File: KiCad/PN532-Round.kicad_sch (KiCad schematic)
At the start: 52 parts, among them J1 Bell, J2 SPOX, SW1 TAMPER, U1 PN532, U2 QR, U3 QR, Y1 27.12MHz

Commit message: Better antennna
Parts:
- removed U3: QR, RevK:QR-PN532, symbol RevK:QR
- added J2: Bell, RevK:PinHeader_1x02_P2.54mm_Vertical_SMD_Pin1Left, symbol Connector:Conn_01x02_Male
- J1: footprint RevK:PinHeader_1x02_P2.54mm_Vertical -> RevK:PinHeader_1x02_P2.54mm_Vertical_SMD_Pin1Right
- J3: renamed from J2; footprint RevK:Molex_MiniSPOX_H4V -> RevK:PinHeader_1x04_P2.54mm_Vertical_SMD_Pin1Right
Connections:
- net GND: now also J2.1 (Pin_1)
- net at R11.2, SW1.2, U1.24 (P30/UART_RX): now also J2.2 (Pin_2)
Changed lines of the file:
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@@
   (junction (at 128.27 118.11) (diameter 0) (color 0 0 0 0)
+  )
+  (junction (at 224.79 25.4) (diameter 0) (color 0 0 0 0)
   )
   (junction (at 231.14 119.38) (diameter 0) (color 0 0 0 0)
@@
     (stroke (width 0) (type default) (color 0 0 0 0))
   )
+  (wire (pts (xy 224.79 25.4) (xy 234.95 25.4))
+    (stroke (width 0) (type default) (color 0 0 0 0))
+  )
   (wire (pts (xy 170.18 74.93) (xy 170.18 80.01))
     (stroke (width 0) (type default) (color 0 0 0 0))
@@
     (stroke (width 0) (type default) (color 0 0 0 0))
   )
-  (wire (pts (xy 224.79 20.32) (xy 224.79 92.71))
-    (stroke (width 0) (type default) (color 0 0 0 0))
-  )
   (wire (pts (xy 237.49 152.4) (xy 246.38 152.4))
     (stroke (width 0) (type default) (color 0 0 0 0))
@@
     (stroke (width 0) (type default) (color 0 0 0 0))
   )
+  (wire (pts (xy 224.79 25.4) (xy 224.79 92.71))
+    (stroke (width 0) (type default) (color 0 0 0 0))
+  )
   (wire (pts (xy 138.43 115.57) (xy 133.35 115.57))
     (stroke (width 0) (type default) (color 0 0 0 0))
@@
   )
   (wire (pts (xy 133.35 115.57) (xy 133.35 127))
+    (stroke (width 0) (type default) (color 0 0 0 0))
+  )
+  (wire (pts (xy 224.79 20.32) (xy 224.79 25.4))
     (stroke (width 0) (type default) (color 0 0 0 0))
   )
@@
   (symbol (lib_id "Connector:Conn_01x04_Male") (at 247.65 78.74 0) (unit 1)
     (in_bom no) (on_board yes)
-    (property "Reference" "J2" (id 0) (at 250.3932 71.6026 0))
+    (property "Reference" "J3" (id 0) (at 250.3932 71.6026 0))
     (property "Value" "SPOX" (id 1) (at 250.3932 73.914 0))
-    (property "Footprint" "RevK:Molex_MiniSPOX_H4V" (id 2) (at 247.65 78.74 0)
+    (property "Footprint" "RevK:PinHeader_1x04_P2.54mm_Vertical_SMD_Pin1Right" (id 2) (at 247.65 78.74 0)
       (effects (font (size 1.27 1.27)) hide)
     )
@@
   (symbol (lib_id "power:GND") (at 252.73 76.2 90) (unit 1)
     (in_bom yes) (on_board yes)
-    (property "Reference" "#PWR041" (id 0) (at 259.08 76.2 0)
+    (property "Reference" "#PWR042" (id 0) (at 259.08 76.2 0)
       (effects (font (size 1.27 1.27)) hide)
     )
@@
   (symbol (lib_id "power:+5V") (at 252.73 78.74 270) (unit 1)
     (in_bom yes) (on_board yes)
-    (property "Reference" "#PWR042" (id 0) (at 248.92 78.74 0)
+    (property "Reference" "#PWR043" (id 0) (at 248.92 78.74 0)
       (effects (font (size 1.27 1.27)) hide)
     )
@@
     (property "Reference" "J1" (id 0) (at 214.8332 145.2626 0))
     (property "Value" "Bell" (id 1) (at 214.8332 147.574 0))
-    (property "Footprint" "RevK:PinHeader_1x02_P2.54mm_Vertical" (id 2) (at 212.09 149.86 0)
+    (property "Footprint" "RevK:PinHeader_1x02_P2.54mm_Vertical_SMD_Pin1Right" (id 2) (at 212.09 149.86 0)
       (effects (font (size 1.27 1.27)) hide)
     )
@@
     )
     (pin "1")
-  )
-  (symbol (lib_id "RevK:QR") (at 281.305 173.355 0) (unit 1)
-    (in_bom no) (on_board yes)
-    (property "Reference" "U3" (id 0) (at 281.305 174.625 0)
-      (effects (font (size 1.27 1.27)) hide)
-    )
-    (property "Value" "QR" (id 1) (at 281.305 174.625 0)
-      (effects (font (size 1.27 1.27)) hide)
-    )
-    (property "Footprint" "RevK:QR-PN532" (id 2) (at 281.305 173.355 0)
-      (effects (font (size 1.27 1.27)) hide)
-    )
-    (property "Datasheet" "" (id 3) (at 281.305 173.355 0)
-      (effects (font (size 1.27 1.27)) hide)
-    )
-    (property "Note" "Non part, PCB printed" (id 4) (at 281.305 173.355 0)
-      (effects (font (size 1.27 1.27)) hide)
-    )
   )
   (symbol (lib_id "Device:R") (at 250.19 152.4 270) (unit 1)
@@
   (symbol (lib_id "power:+3.3V") (at 254 152.4 270) (unit 1)
     (in_bom yes) (on_board yes)
-    (property "Reference" "#PWR043" (id 0) (at 250.19 152.4 0)
+    (property "Reference" "#PWR044" (id 0) (at 250.19 152.4 0)
       (effects (font (size 1.27 1.27)) hide)
     )
@@
   (symbol (lib_id "power:GND") (at 238.76 105.41 0) (mirror y) (unit 1)
     (in_bom yes) (on_board yes)
-    (property "Reference" "#PWR040" (id 0) (at 238.76 111.76 0)
+    (property "Reference" "#PWR041" (id 0) (at 238.76 111.76 0)
       (effects (font (size 1.27 1.27)) hide)
     )
@@
   (symbol (lib_id "power:+3.3V") (at 238.76 90.17 0) (mirror y) (unit 1)
     (in_bom yes) (on_board yes)
-    (property "Reference" "#PWR039" (id 0) (at 238.76 93.98 0)
+    (property "Reference" "#PWR040" (id 0) (at 238.76 93.98 0)
       (effects (font (size 1.27 1.27)) hide)
     )
@@
   (symbol (lib_id "power:GND") (at 234.95 127 0) (unit 1)
     (in_bom yes) (on_board yes)
-    (property "Reference" "#PWR038" (id 0) (at 234.95 133.35 0)
+    (property "Reference" "#PWR039" (id 0) (at 234.95 133.35 0)
       (effects (font (size 1.27 1.27)) hide)
     )
@@
     (pin "~")
   )
+  (symbol (lib_id "power:GND") (at 234.95 27.94 270) (unit 1)
+    (in_bom yes) (on_board yes) (fields_autoplaced)
+    (property "Reference" "#PWR038" (id 0) (at 228.6 27.94 0)
+      (effects (font (size 1.27 1.27)) hide)
+    )
+    (property "Value" "GND" (id 1) (at 231.7751 28.3738 90)
+      (effects (font (size 1.27 1.27)) (justify right))
+    )
+    (property "Footprint" "" (id 2) (at 234.95 27.94 0)
+      (effects (font (size 1.27 1.27)) hide)
+    )
+    (property "Datasheet" "" (id 3) (at 234.95 27.94 0)
+      (effects (font (size 1.27 1.27)) hide)
+    )
+    (pin "1")
+  )
   (symbol (lib_name "Cx2_1") (lib_id "RevK:Cx2") (at 64.77 107.95 0) (unit 1)
     (in_bom yes) (on_board yes)
@@
     )
     (pin "~")
+  )
+  (symbol (lib_id "Connector:Conn_01x02_Male") (at 240.03 27.94 180) (unit 1)
+    (in_bom no) (on_board yes)
+    (property "Reference" "J2" (id 0) (at 237.2868 32.5374 0))
+    (property "Value" "Bell" (id 1) (at 237.2868 30.226 0))
+    (property "Footprint" "RevK:PinHeader_1x02_P2.54mm_Vertical_SMD_Pin1Left" (id 2) (at 240.03 27.94 0)
+      (effects (font (size 1.27 1.27)) hide)
+    )
+    (property "Datasheet" "~" (id 3) (at 240.03 27.94 0)
+      (effects (font (size 1.27 1.27)) hide)
+    )
+    (property "Note" "Non fit" (id 4) (at 240.03 27.94 0)
+      (effects (font (size 1.27 1.27)) hide)
+    )
+    (pin "1")
+    (pin "2")
   )
   (sheet_instances
@@
       (reference "#PWR037") (unit 1) (value "+3.3V") (footprint "")
     )
+    (path "/19af7be6-48e2-46cb-95a1-861bfef57b7e"
+      (reference "#PWR038") (unit 1) (value "GND") (footprint "")
+    )
     (path "/00000000-0000-0000-0000-0000609fd453"
-      (reference "#PWR038") (unit 1) (value "GND") (footprint "")
+      (reference "#PWR039") (unit 1) (value "GND") (footprint "")
     )
     (path "/00000000-0000-0000-0000-0000609cf1cb"
-      (reference "#PWR039") (unit 1) (value "+3.3V") (footprint "")
+      (reference "#PWR040") (unit 1) (value "+3.3V") (footprint "")
     )
     (path "/00000000-0000-0000-0000-0000609ccfd7"
-      (reference "#PWR040") (unit 1) (value "GND") (footprint "")
+      (reference "#PWR041") (unit 1) (value "GND") (footprint "")
     )
     (path "/00000000-0000-0000-0000-0000607d93e3"
-      (reference "#PWR041") (unit 1) (value "GND") (footprint "")
+      (reference "#PWR042") (unit 1) (value "GND") (footprint "")
     )
     (path "/00000000-0000-0000-0000-0000607da4ea"
-      (reference "#PWR042") (unit 1) (value "+5V") (footprint "")
+      (reference "#PWR043") (unit 1) (value "+5V") (footprint "")
     )
     (path "/00000000-0000-0000-0000-000060873918"
-      (reference "#PWR043") (unit 1) (value "+3.3V") (footprint "")
+      (reference "#PWR044") (unit 1) (value "+3.3V") (footprint "")
     )
     (path "/00000000-0000-0000-0000-00006074e4ec"
@@
     )
     (path "/00000000-0000-0000-0000-000060841004"
-      (reference "J1") (unit 1) (value "Bell") (footprint "RevK:PinHeader_1x02_P2.54mm_Vertical")
+      (reference "J1") (unit 1) (value "Bell") (footprint "RevK:PinHeader_1x02_P2.54mm_Vertical_SMD_Pin1Right")
+    )
+    (path "/f91c4452-7b4c-4d66-b5a3-401355df2e4b"
+      (reference "J2") (unit 1) (value "Bell") (footprint "RevK:PinHeader_1x02_P2.54mm_Vertical_SMD_Pin1Left")
     )
     (path "/00000000-0000-0000-0000-0000607d486c"
-      (reference "J2") (unit 1) (value "SPOX") (footprint "RevK:Molex_MiniSPOX_H4V")
+      (reference "J3") (unit 1) (value "SPOX") (footprint "RevK:PinHeader_1x04_P2.54mm_Vertical_SMD_Pin1Right")
     )
     (path "/00000000-0000-0000-0000-0000609405db"
@@
       (reference "U2") (unit 1) (value "QR") (footprint "RevK:QR-PN532")
     )
-    (path "/00000000-0000-0000-0000-000060859564"
-      (reference "U3") (unit 1) (value "QR") (footprint "RevK:QR-PN532")
-    )
     (path "/00000000-0000-0000-0000-00006075caf9"

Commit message: Tidy up and new case
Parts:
- C1, C2: value 160pF 1% -> 160pF; footprint RevK:Cx2_0603 -> RevK:C_0603
- C11, C12, C14, C18, C7, C9: value 0.1uF -> 100nF
- C3, C4: value 22pF 1% -> 22pF
- C8: value 1nF 2% -> 1nF
- J3: value SPOX -> 0.1"; now in the parts list
- R1, R3: footprint RevK:Hidden -> RevK:R_0603_
- R2: footprint RevK:Hidden -> RevK:R_0805_
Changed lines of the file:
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@@
       (effects (font (size 1.27 1.27)) (justify left))
     )
-    (property "Value" "160pF 1%" (id 1) (at 58.42 95.25 0)
-      (effects (font (size 1.27 1.27)) (justify left))
-    )
-    (property "Footprint" "RevK:Cx2_0603" (id 2) (at 65.7352 101.6 0)
+    (property "Value" "160pF" (id 1) (at 58.42 95.25 0)
+      (effects (font (size 1.27 1.27)) (justify left))
+    )
+    (property "Footprint" "RevK:C_0603" (id 2) (at 65.7352 101.6 0)
       (effects (font (size 1.27 1.27)) hide)
     )
@@
     (in_bom yes) (on_board yes)
     (property "Reference" "C3" (id 0) (at 76.2 86.3092 90))
-    (property "Value" "22pF 1%" (id 1) (at 76.2 88.6206 90))
+    (property "Value" "22pF" (id 1) (at 76.2 88.6206 90))
     (property "Footprint" "RevK:C_0603" (id 2) (at 72.39 93.6752 0)
       (effects (font (size 1.27 1.27)) hide)
@@
     (in_bom yes) (on_board yes)
     (property "Reference" "C4" (id 0) (at 76.2 119.4308 90))
-    (property "Value" "22pF 1%" (id 1) (at 76.2 117.1194 90))
+    (property "Value" "22pF" (id 1) (at 76.2 117.1194 90))
     (property "Footprint" "RevK:C_0603" (id 2) (at 80.01 112.0648 0)
       (effects (font (size 1.27 1.27)) hide)
@@
     (in_bom yes) (on_board yes)
     (property "Reference" "C8" (id 0) (at 111.76 132.08 90))
-    (property "Value" "1nF 2%" (id 1) (at 111.76 122.9106 90))
+    (property "Value" "1nF" (id 1) (at 111.76 122.9106 90))
     (property "Footprint" "RevK:C_0603" (id 2) (at 107.95 127.9652 0)
       (effects (font (size 1.27 1.27)) hide)
@@
     (in_bom yes) (on_board yes)
     (property "Reference" "C9" (id 0) (at 118.11 111.7092 90))
-    (property "Value" "0.1uF" (id 1) (at 118.11 114.0206 90))
+    (property "Value" "100nF" (id 1) (at 118.11 114.0206 90))
     (property "Footprint" "RevK:C_0603" (id 2) (at 114.3 119.0752 0)
       (effects (font (size 1.27 1.27)) hide)
@@
       (effects (font (size 1.27 1.27)) (justify left))
     )
-    (property "Value" "0.1uF" (id 1) (at 101.6 82.55 0)
+    (property "Value" "100nF" (id 1) (at 101.6 82.55 0)
       (effects (font (size 1.27 1.27)) (justify left))
     )
@@
       (effects (font (size 1.27 1.27)) (justify left))
     )
-    (property "Value" "0.1uF" (id 1) (at 143.891 72.263 0)
+    (property "Value" "100nF" (id 1) (at 143.891 72.263 0)
       (effects (font (size 1.27 1.27)) (justify left))
     )
@@
       (effects (font (size 1.27 1.27)) (justify left))
     )
-    (property "Value" "0.1uF" (id 1) (at 113.03 55.88 0)
+    (property "Value" "100nF" (id 1) (at 113.03 55.88 0)
       (effects (font (size 1.27 1.27)) (justify left))
     )
@@
       (effects (font (size 1.27 1.27)) (justify left))
     )
-    (property "Value" "0.1uF" (id 1) (at 193.421 115.443 0)
+    (property "Value" "100nF" (id 1) (at 193.421 115.443 0)
       (effects (font (size 1.27 1.27)) (justify left))
     )
@@
       (effects (font (size 1.27 1.27)) (justify left))
     )
-    (property "Value" "0.1uF" (id 1) (at 127.381 143.383 0)
+    (property "Value" "100nF" (id 1) (at 127.381 143.383 0)
       (effects (font (size 1.27 1.27)) (justify left))
     )
@@
   )
   (symbol (lib_id "Connector:Conn_01x04_Male") (at 247.65 78.74 0) (unit 1)
-    (in_bom no) (on_board yes)
+    (in_bom yes) (on_board yes)
     (property "Reference" "J3" (id 0) (at 250.3932 71.6026 0))
-    (property "Value" "SPOX" (id 1) (at 250.3932 73.914 0))
+    (property "Value" "0.1\"" (id 1) (at 250.3932 73.914 0))
     (property "Footprint" "RevK:PinHeader_1x04_P2.54mm_Vertical_SMD_Pin1Right" (id 2) (at 247.65 78.74 0)
       (effects (font (size 1.27 1.27)) hide)
@@
       (effects (font (size 1.27 1.27)) (justify left))
     )
-    (property "Footprint" "RevK:Hidden" (id 2) (at 52.705 105.41 0)
+    (property "Footprint" "RevK:R_0603_" (id 2) (at 52.705 105.41 0)
       (effects (font (size 1.27 1.27)) hide)
     )
@@
       (effects (font (size 1.27 1.27)) (justify left))
     )
-    (property "Value" "160pF 1%" (id 1) (at 58.42 105.41 0)
-      (effects (font (size 1.27 1.27)) (justify left))
-    )
-    (property "Footprint" "RevK:Cx2_0603" (id 2) (at 65.7352 111.76 0)
+    (property "Value" "160pF" (id 1) (at 58.42 105.41 0)
+      (effects (font (size 1.27 1.27)) (justify left))
+    )
+    (property "Footprint" "RevK:C_0603" (id 2) (at 65.7352 111.76 0)
       (effects (font (size 1.27 1.27)) hide)
     )
@@
       (effects (font (size 1.27 1.27)) (justify left))
     )
-    (property "Footprint" "RevK:Hidden" (id 2) (at 52.705 100.33 0)
+    (property "Footprint" "RevK:R_0603_" (id 2) (at 52.705 100.33 0)
       (effects (font (size 1.27 1.27)) hide)
     )
@@
       (effects (font (size 1.27 1.27)) (justify left))
     )
-    (property "Footprint" "RevK:Hidden" (id 2) (at 52.705 102.87 0)
+    (property "Footprint" "RevK:R_0805_" (id 2) (at 52.705 102.87 0)
       (effects (font (size 1.27 1.27)) hide)
     )
@@
     )
     (path "/00000000-0000-0000-0000-000060756cae"
-      (reference "C1") (unit 1) (value "160pF 1%") (footprint "RevK:Cx2_0603")
+      (reference "C1") (unit 1) (value "160pF") (footprint "RevK:C_0603")
     )
     (path "/4b8d25e0-f830-4864-9f16-698fc7486e15"
-      (reference "C2") (unit 1) (value "160pF 1%") (footprint "RevK:Cx2_0603")
+      (reference "C2") (unit 1) (value "160pF") (footprint "RevK:C_0603")
     )
     (path "/00000000-0000-0000-0000-000060758ce7"
-      (reference "C3") (unit 1) (value "22pF 1%") (footprint "RevK:C_0603")
+      (reference "C3") (unit 1) (value "22pF") (footprint "RevK:C_0603")
     )
     (path "/00000000-0000-0000-0000-000060759861"
-      (reference "C4") (unit 1) (value "22pF 1%") (footprint "RevK:C_0603")
+      (reference "C4") (unit 1) (value "22pF") (footprint "RevK:C_0603")
     )
     (path "/00000000-0000-0000-0000-00006075a7aa"
@@
     )
     (path "/00000000-0000-0000-0000-00006075fd74"
-      (reference "C7") (unit 1) (value "0.1uF") (footprint "RevK:C_0603")
+      (reference "C7") (unit 1) (value "100nF") (footprint "RevK:C_0603")
     )
     (path "/00000000-0000-0000-0000-00006075c646"
-      (reference "C8") (unit 1) (value "1nF 2%") (footprint "RevK:C_0603")
+      (reference "C8") (unit 1) (value "1nF") (footprint "RevK:C_0603")
     )
     (path "/00000000-0000-0000-0000-00006075d8ac"
-      (reference "C9") (unit 1) (value "0.1uF") (footprint "RevK:C_0603")
+      (reference "C9") (unit 1) (value "100nF") (footprint "RevK:C_0603")
     )
     (path "/00000000-0000-0000-0000-00006075f2fd"
@@
     )
     (path "/00000000-0000-0000-0000-0000607617f2"
-      (reference "C11") (unit 1) (value "0.1uF") (footprint "RevK:C_0603")
+      (reference "C11") (unit 1) (value "100nF") (footprint "RevK:C_0603")
     )
     (path "/00000000-0000-0000-0000-00006078de67"
-      (reference "C12") (unit 1) (value "0.1uF") (footprint "RevK:C_0603")
+      (reference "C12") (unit 1) (value "100nF") (footprint "RevK:C_0603")
     )
     (path "/00000000-0000-0000-0000-000060761b18"
@@
     )
     (path "/00000000-0000-0000-0000-0000607608e5"
-      (reference "C14") (unit 1) (value "0.1uF") (footprint "RevK:C_0603")
+      (reference "C14") (unit 1) (value "100nF") (footprint "RevK:C_0603")
     )
     (path "/00000000-0000-0000-0000-000060993dc2"
@@
     )
     (path "/00000000-0000-0000-0000-0000607627aa"
-      (reference "C18") (unit 1) (value "0.1uF") (footprint "RevK:C_0603")
+      (reference "C18") (unit 1) (value "100nF") (footprint "RevK:C_0603")
     )
     (path "/00000000-0000-0000-0000-0000609f7a83"
@@
     )
     (path "/00000000-0000-0000-0000-0000607d486c"
-      (reference "J3") (unit 1) (value "SPOX") (footprint "RevK:PinHeader_1x04_P2.54mm_Vertical_SMD_Pin1Right")
+      (reference "J3") (unit 1) (value "0.1\"") (footprint "RevK:PinHeader_1x04_P2.54mm_Vertical_SMD_Pin1Right")
     )
     (path "/00000000-0000-0000-0000-0000609405db"
@@
     )
     (path "/9d1ee0b7-8453-459c-a833-897b79b8b1c4"
-      (reference "R1") (unit 1) (value "0R") (footprint "RevK:Hidden")
+      (reference "R1") (unit 1) (value "0R") (footprint "RevK:R_0603_")
     )
     (path "/dc84d5ee-d81a-4f4d-a75f-84acaaa9d309"
-      (reference "R2") (unit 1) (value "0R") (footprint "RevK:Hidden")
+      (reference "R2") (unit 1) (value "0R") (footprint "RevK:R_0805_")
     )
     (path "/01990a6a-0667-4329-811a-e07a4a9e79e9"
-      (reference "R3") (unit 1) (value "0R") (footprint "RevK:Hidden")
+      (reference "R3") (unit 1) (value "0R") (footprint "RevK:R_0603_")
     )
     (path "/00000000-0000-0000-0000-00006075de03"

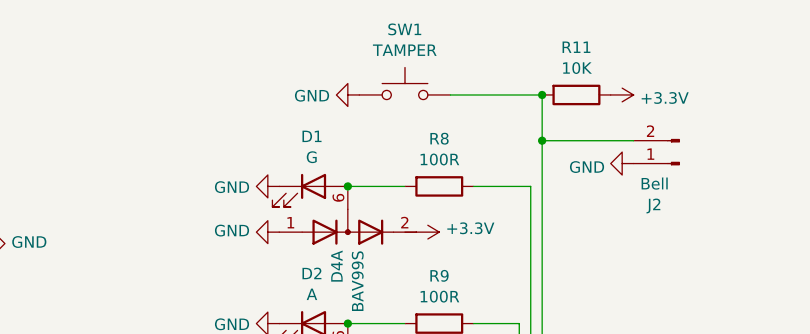
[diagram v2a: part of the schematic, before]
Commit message: Proper tamper switch
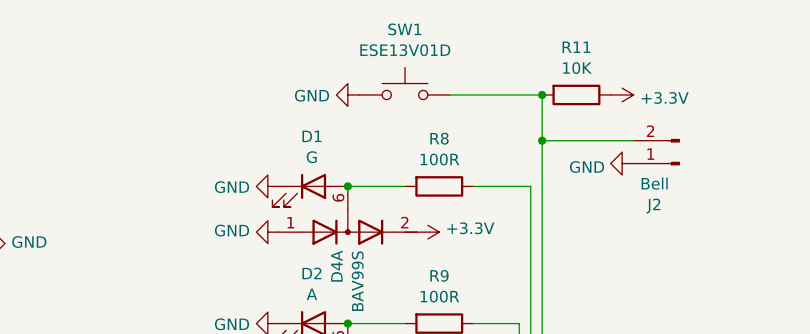
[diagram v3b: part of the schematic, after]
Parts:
- SW1: value TAMPER -> ESE13V01D; footprint RevK:SW_PUSH_6mm_SMD -> RevK:ESE13; Manufacturer E-Switch -> Panasonic; Part No LL3301NF065QG -> ESE13V01D; now in the parts list
- Y1: footprint RevK:Crystal-3.4x2.7 -> RevK:Crystal-3.2x2.5
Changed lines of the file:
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@@
       (effects (font (size 1.27 1.27)) (justify left))
     )
-    (property "Footprint" "RevK:Crystal-3.4x2.7" (id 2) (at 158.75 144.78 0)
+    (property "Footprint" "RevK:Crystal-3.2x2.5" (id 2) (at 158.75 144.78 0)
       (effects (font (size 1.27 1.27)) hide)
     )
@@
   )
   (symbol (lib_id "Switch:SW_Push") (at 209.55 20.32 0) (unit 1)
-    (in_bom no) (on_board yes)
+    (in_bom yes) (on_board yes)
     (property "Reference" "SW1" (id 0) (at 209.55 13.081 0))
-    (property "Value" "TAMPER" (id 1) (at 209.55 15.3924 0))
-    (property "Footprint" "RevK:SW_PUSH_6mm_SMD" (id 2) (at 209.55 15.24 0)
-      (effects (font (size 1.27 1.27)) hide)
-    )
-    (property "Datasheet" "https://www.mouser.co.uk/ProductDetail/612-LL3301NF065QG" (id 3) (at 209.55 15.24 0)
-      (effects (font (size 1.27 1.27)) hide)
-    )
-    (property "Part No" "LL3301NF065QG" (id 4) (at 209.55 20.32 0)
-      (effects (font (size 1.27 1.27)) hide)
-    )
-    (property "Manufacturer" "E-Switch" (id 5) (at 209.55 20.32 0)
+    (property "Value" "ESE13V01D" (id 1) (at 209.55 15.3924 0))
+    (property "Footprint" "RevK:ESE13" (id 2) (at 209.55 15.24 0)
+      (effects (font (size 1.27 1.27)) hide)
+    )
+    (property "Datasheet" "https://docs.rs-online.com/73f9/0900766b810acfc9.pdf" (id 3) (at 209.55 15.24 0)
+      (effects (font (size 1.27 1.27)) hide)
+    )
+    (property "Part No" "ESE13V01D" (id 4) (at 209.55 20.32 0)
+      (effects (font (size 1.27 1.27)) hide)
+    )
+    (property "Manufacturer" "Panasonic" (id 5) (at 209.55 20.32 0)
       (effects (font (size 1.27 1.27)) hide)
     )
@@
     )
     (path "/00000000-0000-0000-0000-00006076e91e"
-      (reference "SW1") (unit 1) (value "TAMPER") (footprint "RevK:SW_PUSH_6mm_SMD")
+      (reference "SW1") (unit 1) (value "ESE13V01D") (footprint "RevK:ESE13")
     )
     (path "/00000000-0000-0000-0000-000060753706"
@@
     )
     (path "/00000000-0000-0000-0000-00006075caf9"
-      (reference "Y1") (unit 1) (value "27.12MHz") (footprint "RevK:Crystal-3.4x2.7")
-    )
-  )
+      (reference "Y1") (unit 1) (value "27.12MHz") (footprint "RevK:Crystal-3.2x2.5")
+    )
+  )
